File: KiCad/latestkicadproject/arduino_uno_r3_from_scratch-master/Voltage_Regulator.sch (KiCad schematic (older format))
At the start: 8 parts, among them IC1 MC33269ST-5.OT3, IC2 MC33269ST-5.OT3, X2 DG3XX-02-3.5

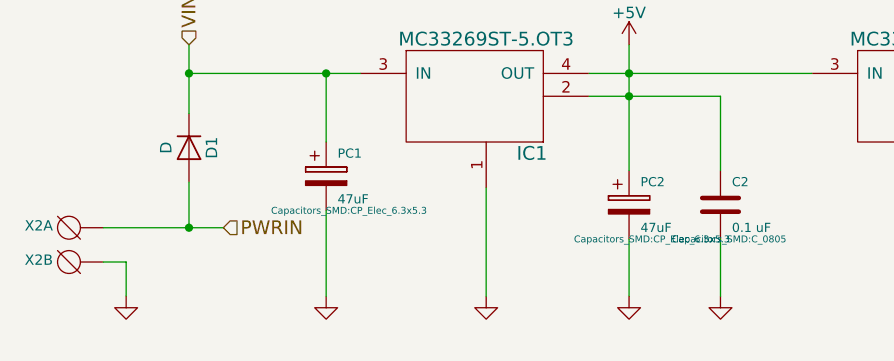
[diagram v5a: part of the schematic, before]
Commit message: correctie gnd-fouten
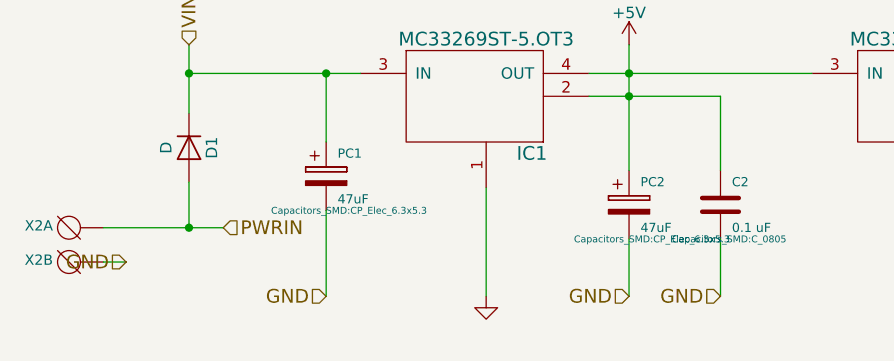
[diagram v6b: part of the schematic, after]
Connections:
- net GND: now also C2.2, PC1.2, PC2.2, X2.2 (KL)
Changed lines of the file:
@@
 $Comp
 L GND-RESCUE-Arduino_Uno_R3_From_Scratch #PWR01
-U 1 1 561FCF65
-P 5025 4400
-F 0 "#PWR01" H 5025 4150 50  0001 C CNN
-F 1 "GND" H 5025 4250 50  0001 C CNN
-F 2 "" H 5025 4400 60  0000 C CNN
-F 3 "" H 5025 4400 60  0000 C CNN
-F 4 "ANY" H 5025 4400 60  0001 C CNN "Source"
-F 5 "N" H 5025 4400 60  0001 C CNN "Critical"
-F 6 "~" H 5025 4400 60  0001 C CNN "Notes"
-	1    5025 4400
-	1    0    0    -1
-$EndComp
-$Comp
-L GND-RESCUE-Arduino_Uno_R3_From_Scratch #PWR02
 U 1 1 561FEA9F
 P 5725 4400
-F 0 "#PWR02" H 5725 4150 50  0001 C CNN
+F 0 "#PWR01" H 5725 4150 50  0001 C CNN
 F 1 "GND" H 5725 4250 50  0001 C CNN
 F 2 "" H 5725 4400 60  0000 C CNN
@@
 F 6 "~" H 5725 4400 60  0001 C CNN "Notes"
 	1    5725 4400
-	1    0    0    -1
-$EndComp
-$Comp
-L GND-RESCUE-Arduino_Uno_R3_From_Scratch #PWR03
-U 1 1 561FEAC8
-P 6350 4400
-F 0 "#PWR03" H 6350 4150 50  0001 C CNN
-F 1 "GND" H 6350 4250 50  0001 C CNN
-F 2 "" H 6350 4400 60  0000 C CNN
-F 3 "" H 6350 4400 60  0000 C CNN
-F 4 "ANY" H 6350 4400 60  0001 C CNN "Source"
-F 5 "N" H 6350 4400 60  0001 C CNN "Critical"
-F 6 "~" H 6350 4400 60  0001 C CNN "Notes"
-	1    6350 4400
-	1    0    0    -1
-$EndComp
-$Comp
-L GND-RESCUE-Arduino_Uno_R3_From_Scratch #PWR04
-U 1 1 561FEB19
-P 6750 4400
-F 0 "#PWR04" H 6750 4150 50  0001 C CNN
-F 1 "GND" H 6750 4250 50  0001 C CNN
-F 2 "" H 6750 4400 60  0000 C CNN
-F 3 "" H 6750 4400 60  0000 C CNN
-F 4 "ANY" H 6750 4400 60  0001 C CNN "Source"
-F 5 "N" H 6750 4400 60  0001 C CNN "Critical"
-F 6 "~" H 6750 4400 60  0001 C CNN "Notes"
-	1    6750 4400
-	1    0    0    -1
-$EndComp
-$Comp
-L GND-RESCUE-Arduino_Uno_R3_From_Scratch #PWR05
-U 1 1 56209A71
-P 4150 4400
-F 0 "#PWR05" H 4150 4150 50  0001 C CNN
-F 1 "GND" H 4150 4250 50  0001 C CNN
-F 2 "" H 4150 4400 60  0000 C CNN
-F 3 "" H 4150 4400 60  0000 C CNN
-F 4 "ANY" H 4150 4400 60  0001 C CNN "Source"
-F 5 "N" H 4150 4400 60  0001 C CNN "Critical"
-F 6 "~" H 4150 4400 60  0001 C CNN "Notes"
-	1    4150 4400
 	1    0    0    -1
 $EndComp
@@
 	6750 3525 6750 3850
 $Comp
-L GND #PWR06
+L GND #PWR02
 U 1 1 5AA01DB9
 P 7700 4400
-F 0 "#PWR06" H 7700 4150 50  0001 C CNN
+F 0 "#PWR02" H 7700 4150 50  0001 C CNN
 F 1 "GND" H 7700 4250 50  0000 C CNN
 F 2 "" H 7700 4400 50  0001 C CNN
@@
 $EndComp
 $Comp
-L GND #PWR07
+L GND #PWR03
 U 1 1 5AA02AAE
 P 8850 4400
-F 0 "#PWR07" H 8850 4150 50  0001 C CNN
+F 0 "#PWR03" H 8850 4150 50  0001 C CNN
 F 1 "GND" H 8850 4250 50  0000 C CNN
 F 2 "" H 8850 4400 50  0001 C CNN
@@
 	8850 4075 8850 4400
 $Comp
-L +5V #PWR08
+L +5V #PWR04
 U 1 1 5AA0368C
 P 6350 3300
-F 0 "#PWR08" H 6350 3150 50  0001 C CNN
+F 0 "#PWR04" H 6350 3150 50  0001 C CNN
 F 1 "+5V" H 6350 3440 50  0000 C CNN
 F 2 "" H 6350 3300 50  0001 C CNN
@@
 Text HLabel 8675 3350 1    60   Input ~ 0
 +3V3
-Wire Wire Line
-	4150 4250 4150 4400
 $Comp
 L DG3XX-02-3.5 X2
@@
 	8250 3525 8250 3425
 Connection ~ 8250 3425
+Text HLabel 4150 4250 0    60   Input ~ 0
+GND
+Text HLabel 6750 4400 0    60   Input ~ 0
+GND
+Text HLabel 6350 4400 0    60   Input ~ 0
+GND
+Text HLabel 5025 4400 0    60   Input ~ 0
+GND
 $EndSCHEMATC

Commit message: verbeteringen kicad
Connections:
- net GND: now also IC1.1
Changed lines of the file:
@@
-	1    0    0    -1
-$EndComp
-$Comp
-L GND-RESCUE-Arduino_Uno_R3_From_Scratch #PWR01
-U 1 1 561FEA9F
-P 5725 4400
-F 0 "#PWR01" H 5725 4150 50  0001 C CNN
-F 1 "GND" H 5725 4250 50  0001 C CNN
-F 2 "" H 5725 4400 60  0000 C CNN
-F 3 "" H 5725 4400 60  0000 C CNN
-F 4 "ANY" H 5725 4400 60  0001 C CNN "Source"
-F 5 "N" H 5725 4400 60  0001 C CNN "Critical"
-F 6 "~" H 5725 4400 60  0001 C CNN "Notes"
-	1    5725 4400
 	1    0    0    -1
 $EndComp
@@
 	6750 3525 6750 3850
 $Comp
-L GND #PWR02
-U 1 1 5AA01DB9
-P 7700 4400
-F 0 "#PWR02" H 7700 4150 50  0001 C CNN
-F 1 "GND" H 7700 4250 50  0000 C CNN
-F 2 "" H 7700 4400 50  0001 C CNN
-F 3 "" H 7700 4400 50  0001 C CNN
-	1    7700 4400
-	1    0    0    -1
-$EndComp
-$Comp
 L C C3
 U 1 1 5AA02A53
@@
 F 12 "~" H 8850 3925 60  0001 C CNN "Notes"
 	1    8850 3925
-	1    0    0    -1
-$EndComp
-$Comp
-L GND #PWR03
-U 1 1 5AA02AAE
-P 8850 4400
-F 0 "#PWR03" H 8850 4150 50  0001 C CNN
-F 1 "GND" H 8850 4250 50  0000 C CNN
-F 2 "" H 8850 4400 50  0001 C CNN
-F 3 "" H 8850 4400 50  0001 C CNN
-	1    8850 4400
 	1    0    0    -1
 $EndComp
@@
 Text HLabel 5025 4400 0    60   Input ~ 0
 GND
+Text HLabel 5725 4400 0    60   Input ~ 0
+GND
+Text HLabel 7700 4400 0    60   Input ~ 0
+GND
+Text HLabel 8850 4400 0    60   Input ~ 0
+GND
 $EndSCHEMATC

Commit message: PCBtotaal
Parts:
- D1: footprint Diodes_SMD:D_MicroMELF_Hadsoldering -> Diodes_SMD:D_MiniMELF_Handsoldering
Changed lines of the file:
@@
 F 0 "D1" H 4425 3850 50  0000 C CNN
 F 1 "D" H 4425 3650 50  0000 C CNN
-F 2 "Diodes_SMD:D_MicroMELF_Hadsoldering" H 4425 3750 50  0001 C CNN
+F 2 "Diodes_SMD:D_MiniMELF_Handsoldering" H 4425 3750 50  0001 C CNN
 F 3 "" H 4425 3750 50  0001 C CNN
 	1    4425 3750
@@
 	8850 4075 8850 4400
 $Comp
-L +5V #PWR04
+L +5V #PWR01
 U 1 1 5AA0368C
 P 6350 3300
-F 0 "#PWR04" H 6350 3150 50  0001 C CNN
+F 0 "#PWR01" H 6350 3150 50  0001 C CNN
 F 1 "+5V" H 6350 3440 50  0000 C CNN
 F 2 "" H 6350 3300 50  0001 C CNN
